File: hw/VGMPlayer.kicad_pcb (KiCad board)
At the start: 4 copper layers, 40 x 67 mm, 99 parts, among them J1 Micro_SD_Card, J2 EarPiece, P1 USB_C_Receptacle_16P, P2 SWD, P3 BATT, P5 ICSP, P6 CODEC, Q1 AO3401A, Q2 AO3401A, Q3 2N7002, Q4 2N7002, U1 RP2040, U2 W25QxxJVZP, U3 LP5907MFX-3.3, U4 WM8978, U5 MCP73831-OT, U6 PIC16F1503-IMG, U7 LP5907MFX-3.3, Y1 12MHz

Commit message: Rename button labels
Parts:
- S1: value L -> M
- S2: value R -> P

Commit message: Using Linux Kicad 6.0.1
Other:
- net class Default removed
- net class Power removed

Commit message: V4 hardware
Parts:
- removed C14: 1u, BZ_Capacitor:C_0603
- removed the C17 at (138.4, 109.3)
- removed the C19 at (136.6, 119.0)
- removed the C23 at (131.6, 111.7)
- removed the C24 at (134.8, 116.8)
- removed the C27 at (140.1, 118.8)
- removed the C30 at (145.1, 134.2)
- removed JP1: Jumper-NC, BZ_Misc:Jumper-Solder
- removed JP2, JP3: Jumper-NO, BZ_Misc:Jumper-Solder
- removed R13: 1K, BZ_Resistor:R_0402
- removed the U3 at (134.3, 113.9)
- added C20: 1u, BZ_Capacitor:C_0603, B.Cu at (135.0, 120.8)
- added U4: MAX9890BETA, BZ_Standard_IC:TDFN-8-1EP_3x3x0.65P_EP2.3x1.5, B.Cu at (136.5, 118.1)
- added kibuzzard-62236962: G***, kibuzzard-62236962, F.Cu at (157.1, 141.0)
- C15: renamed from C25; value 10u -> 4.7u
- C16: renamed from C18; value 10u -> 4.7u
- C17: renamed from C20; value 10u -> 4.7u
- C18: renamed from C22; value 10u -> 4.7u
- C19: renamed from C26; value 10u -> 4.7u
- S1: value M -> B
- S2: value P -> F
- S5: value RESET -> P; footprint BZ_Switch:SW-PUSH_4x3x2H -> VGMPlayer:MultiButton; moved to F.Cu
- moved C15 13.0 mm to (142.3, 108.7), turned to 90 degrees
- moved S3 13.0 mm to (140.0, 132.3), turned to 90 degrees
- moved C18 11.2 mm to (132.3, 115.9), turned to 180 degrees
- moved C19 8.18 mm to (132.3, 114.5), turned to 180 degrees
- moved S5 8.02 mm to (160.0, 123.5), turned to -90 degrees
- moved C17 6.49 mm to (132.3, 113.1), turned to 180 degrees
- moved S2 5.03 mm to (160.0, 132.3)
- moved S1 4.27 mm to (140.0, 123.5)
- moved C16 3.95 mm to (143.7, 108.7)
- moved C21 3.94 mm to (138.1, 120.8), turned to 180 degrees
- moved S4 3.10 mm to (150.0, 127.9)
- moved U3 2.92 mm to (138.3, 111.6), turned to 45 degrees
- moved FB1 2.31 mm to (132.0, 110.3), turned to 180 degrees
- moved R15 1.60 mm to (143.1, 133.4)
- moved R17 1.60 mm to (143.1, 135.0)
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- renumbered C28 to C22, C29 to C23, C16 to C24, C31 to C25, C33 to C26, C34 to C27, C35 to C28, C32 to C29, C36 to C30, U4 to U3
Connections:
- C15 pad 1: VDDA -> 3V3
- C17 pad 1: VDDA -> /AVDD
- C18 pad 1: Net-(C21-Pad1) -> VIN
- C22 pad 1: Net-(C28-Pad1) -> Net-(C22-Pad1)
- C23 pad 1: Net-(C29-Pad1) -> Net-(C23-Pad1)
- C26 pad 1: Net-(C33-Pad1) -> VIN
- FB1 pad 1: Net-(C21-Pad1) -> /AVDD
- FB1 pad 2: VIN -> 3V3
- P1 pad A8: (no net) -> unconnected-(P1-PadA8)
- P1 pad B8: (no net) -> unconnected-(P1-PadB8)
- P2 pad 6: (no net) -> unconnected-(P2-Pad6)
- P2 pad 7: (no net) -> unconnected-(P2-Pad7)
- P5 pad 6: (no net) -> unconnected-(P5-Pad6)
- Q2 pad 3: Net-(C33-Pad1) -> VIN
- U1 pad 29: (no net) -> unconnected-(U1-Pad29)
- U1 pad 30: (no net) -> unconnected-(U1-Pad30)
- U1 pad 31: Net-(R13-Pad2) -> /OUTEN
- U1 pad 38: (no net) -> /JACK_DET
- U1 pad 39: (no net) -> unconnected-(U1-Pad39)
- U1 pad 40: (no net) -> unconnected-(U1-Pad40)
- U1 pad 41: (no net) -> unconnected-(U1-Pad41)
- U3 pad 1: (no net) -> unconnected-(U3-Pad1)
- U3 pad 15: (no net) -> unconnected-(U3-Pad15)
- U3 pad 19: /BEEP -> unconnected-(U3-Pad19)
- U3 pad 2: (no net) -> unconnected-(U3-Pad2)
- U3 pad 20: (no net) -> unconnected-(U3-Pad20)
- U3 pad 21: (no net) -> unconnected-(U3-Pad21)
- U3 pad 22: (no net) -> unconnected-(U3-Pad22)
- U3 pad 26: Net-(C21-Pad1) -> VIN
- U3 pad 29: Net-(C28-Pad1) -> Net-(U3-Pad29)
- U3 pad 30: Net-(C29-Pad1) -> Net-(U3-Pad30)
- U3 pad 31: VDDA -> /AVDD
- U3 pad 32: (no net) -> unconnected-(U3-Pad32)
- U3 pad 4: (no net) -> unconnected-(U3-Pad4)
- U3 pad 5: (no net) -> unconnected-(U3-Pad5)
- U3 pad 6: (no net) -> unconnected-(U3-Pad6)
- U3 pad 9: (no net) -> unconnected-(U3-Pad9)
- U7 pad 1: Net-(C33-Pad1) -> VIN
- U7 pad 3: Net-(C33-Pad1) -> VIN
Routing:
- net 3V3: track 109.5 -> 156.2 mm
- net Net-(C21-Pad1): track 31.0 -> 1.95 mm, vias 2 -> 0
- net VIN: track 23.6 -> 45.6 mm
- net /OUTEN: track 0.00 -> 21.4 mm, vias 0 -> 2
- net /AVDD: track 0.00 -> 16.9 mm, vias 0 -> 2
- net Net-(R13-Pad2): track 15.8 -> 0.00 mm, vias 2 -> 0
- net Net-(C33-Pad1): track 14.7 -> 0.00 mm, vias 2 -> 0
- net VDDA: track 12.2 -> 0.00 mm
- net /ICSPCLK: track 43.5 -> 55.7 mm
- net Net-(C29-Pad1): track 11.8 -> 0.00 mm
- net Net-(C28-Pad1): track 10.8 -> 0.00 mm
- net Net-(U3-Pad29): track 0.00 -> 8.80 mm, vias 0 -> 2
- net Net-(C23-Pad1): track 0.00 -> 8.52 mm
- net Net-(C22-Pad1): track 0.00 -> 7.86 mm
- net /VPP: track 34.4 -> 41.9 mm
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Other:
- rule solder_mask_min_width: 0.08 -> 0.2
- board text added: "20220305"
- board text removed: "20210714"

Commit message: V4 hardware send for JLC
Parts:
- removed the C27 at (155.6, 96.8)
- removed Q2: AO3401A, BZ_Standard_IC:SOT-23-3
- removed R20: 100K, BZ_Resistor:R_0402
- added C29: 4.7u, BZ_Capacitor:C_0603, B.Cu at (156.1, 95.3)
- added R13: 10K, BZ_Resistor:R_0402, B.Cu at (132.3, 118.0)
- C26: value 1u -> 4.7u
- R21: value 10K -> 100K
- S1: value B -> U
- S2: value F -> B
- S3: value U -> D
- S4: value D -> P
- S5: value P -> F
- U7: value LP5907MFX-3.3 -> XC6220B331MR
- moved C25 7.52 mm to (156.1, 104.0), turned to 180 degrees
- moved C26 4.17 mm to (156.1, 97.4), turned to 180 degrees
- moved R18 2.58 mm to (159.4, 98.4), turned to -90 degrees
- moved S1 2.26 mm to (139.5, 121.3)
- moved S5 2.26 mm to (160.5, 121.3)
- moved D2 1.90 mm to (159.2, 102.5)
- moved R21 1.60 mm to (153.0, 104.2), turned to -90 degrees
- moved R23 1.50 mm to (153.0, 102.1)
- moved R24 1.40 mm to (153.0, 100.0)
- moved C28 1.30 mm to (153.0, 97.9)
- moved S4 1.00 mm to (150.0, 126.9)
- moved U7 1.00 mm to (156.1, 100.7)
- moved S2 0.54 mm to (160.5, 132.5)
- moved S3 0.54 mm to (139.5, 132.5)
- moved R15 0.50 mm to (143.1, 132.9)
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- renumbered C15 to C14, C16 to C15, C17 to C16, C18 to C17, C20 to C18, C21 to C19, C19 to C20, C22 to C21, C23 to C22, C24 to C23, C25 to C24, C28 to C25, C29 to C27, C30 to C28
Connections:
- C17 pad 1: VIN -> /AVDD
- C25 pad 1: 3V3 -> VRAW
- C26 pad 1: VIN -> 3V3
- R21 pad 1: Net-(Q2-Pad1) -> Net-(R21-Pad1)
- R21 pad 2: Net-(R21-Pad2) -> GND
- U3 pad 26: VIN -> /AVDD
- U6 pad 7: Net-(R21-Pad2) -> Net-(R21-Pad1)
- U7 pad 1: VIN -> VRAW
- U7 pad 3: VIN -> Net-(R21-Pad1)
- U7 pad 4: Net-(C27-Pad1) -> unconnected-(U7-Pad4)
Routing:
- net VIN: track 45.6 -> 0.00 mm, vias 2 -> 0
- net 3V3: track 156.2 -> 141.1 mm, vias 15 -> 16
- net GND: track 219.3 -> 230.7 mm, vias 79 -> 77
- net Net-(Q2-Pad1): track 6.19 -> 0.00 mm
- net Net-(R21-Pad1): track 0.00 -> 5.33 mm
- net VRAW: track 45.3 -> 41.5 mm
- net /OUTEN: track 21.4 -> 25.0 mm, vias 2 -> 3
- net Net-(R21-Pad2): track 3.19 -> 0.00 mm
- net /AVDD: track 16.9 -> 20.0 mm, vias 2 -> 3
- net /VPP: track 41.9 -> 39.4 mm
- net /BATT: track 33.3 -> 31.4 mm
- net Net-(C28-Pad1): track 10.1 -> 8.37 mm
- net Net-(C27-Pad1): track 1.35 -> 0.00 mm
- net /ICSPDAT: track 56.6 -> 55.4 mm
- net Net-(S4-Pad2): track 30.1 -> 29.1 mm
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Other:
- rule pad_to_mask_clearance: 0.05 -> 0
- board text added: "20220306"
- board text removed: "20220305"

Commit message: Use new iPhone8 measurement
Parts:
- U5: value MCP73831-OT -> MCP73832-OT
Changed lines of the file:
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@@
       (effects (font (size 0.8 0.8) (thickness 0.15)) (justify mirror))
     )
-    (fp_text value "MCP73831-OT" (at 0 -2.6) (layer "B.Fab") hide
+    (fp_text value "MCP73832-OT" (at 0 -2.6) (layer "B.Fab") hide
       (effects (font (size 0.8 0.8) (thickness 0.15)) (justify mirror))
     )

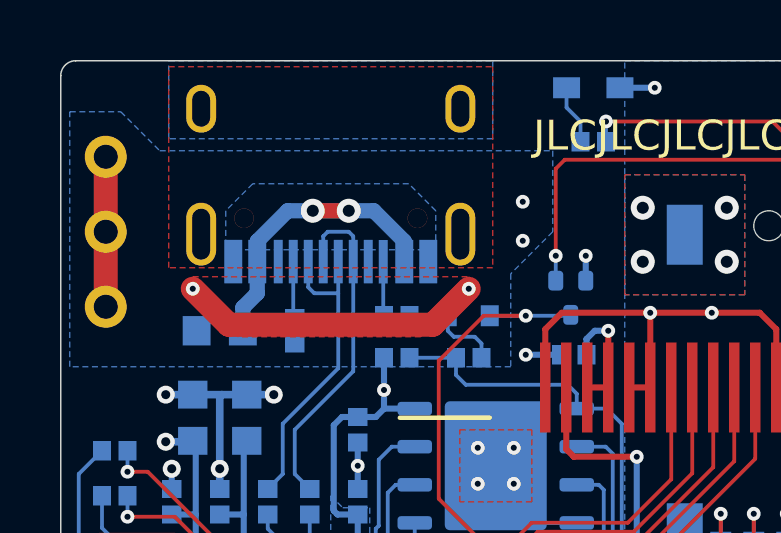
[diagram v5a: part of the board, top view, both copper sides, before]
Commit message: Update switch names
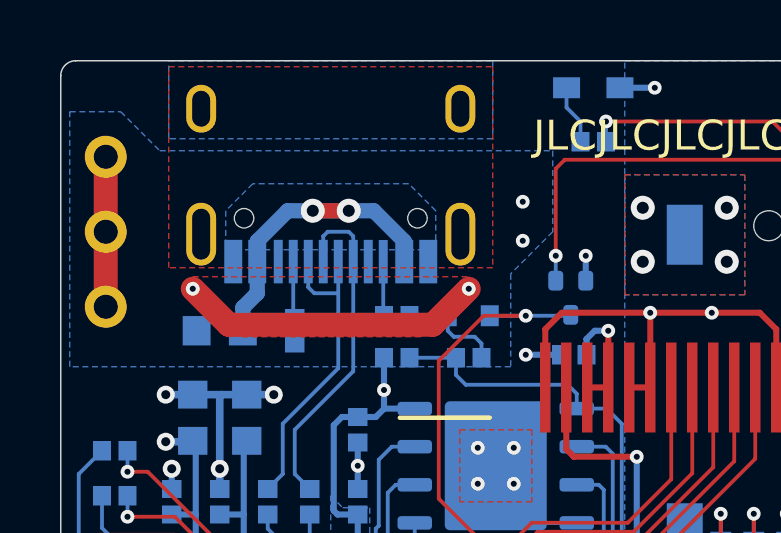
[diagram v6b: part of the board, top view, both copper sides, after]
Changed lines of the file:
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@@
     (property "Sheetname" "")
     (attr smd)
-    (fp_text reference "P1" (at 0 9.6) (layer "B.SilkS") hide
+    (fp_text reference "P1" (at 0 9.6 180) (layer "B.SilkS") hide
       (effects (font (size 0.8 0.8) (thickness 0.15)) (justify mirror))
     )
-    (fp_text value "USB_C_Receptacle_16P" (at 0 -1.5) (layer "B.Fab") hide
+    (fp_text value "USB_C_Receptacle_16P" (at 0 -1.5 180) (layer "B.Fab") hide
       (effects (font (size 1 1) (thickness 0.15)) (justify mirror))
     )
-    (fp_text user "${REFERENCE}" (at 0 6.7) (layer "B.Fab")
+    (fp_text user "${REFERENCE}" (at 0 6.7 180) (layer "B.Fab")
       (effects (font (size 0.8 0.8) (thickness 0.15)) (justify mirror))
     )
@@
     (fp_line (start 4.47 7.3) (end -4.47 7.3) (layer "B.Fab") (width 0.1))
     (fp_line (start -4.47 7.3) (end -4.47 0) (layer "B.Fab") (width 0.1))
-    (pad "A1" smd rect locked (at -3.25 7.695) (size 0.6 1.45) (layers "B.Cu" "B.Paste" "B.Mask")
+    (pad "" np_thru_hole oval (at 2.89 6.25) (size 0.65 0.65) (drill 0.65) (layers F&B.Cu *.Mask))
+    (pad "" np_thru_hole oval (at -2.89 6.25) (size 0.65 0.65) (drill 0.65) (layers F&B.Cu *.Mask))
+    (pad "A1" smd rect (at -3.25 7.695) (size 0.6 1.45) (layers "B.Cu" "B.Paste" "B.Mask")
       (net 1 "GND") (pinfunction "GND") (pintype "passive"))
-    (pad "A4" smd rect locked (at -2.45 7.695) (size 0.6 1.45) (layers "B.Cu" "B.Paste" "B.Mask")
+    (pad "A4" smd rect (at -2.45 7.695) (size 0.6 1.45) (layers "B.Cu" "B.Paste" "B.Mask")
       (net 2 "VUSB") (pinfunction "VBUS") (pintype "passive"))
-    (pad "A5" smd rect locked (at -1.25 7.695) (size 0.3 1.45) (layers "B.Cu" "B.Paste" "B.Mask")
+    (pad "A5" smd rect (at -1.25 7.695) (size 0.3 1.45) (layers "B.Cu" "B.Paste" "B.Mask")
       (net 8 "Net-(P1-PadA5)") (pinfunction "CC1") (pintype "bidirectional"))
-    (pad "A6" smd rect locked (at -0.25 7.695) (size 0.3 1.45) (layers "B.Cu" "B.Paste" "B.Mask")
+    (pad "A6" smd rect (at -0.25 7.695) (size 0.3 1.45) (layers "B.Cu" "B.Paste" "B.Mask")
       (net 6 "Net-(P1-PadA6)") (pinfunction "D+") (pintype "bidirectional"))
-    (pad "A7" smd rect locked (at 0.25 7.695) (size 0.3 1.45) (layers "B.Cu" "B.Paste" "B.Mask")
+    (pad "A7" smd rect (at 0.25 7.695) (size 0.3 1.45) (layers "B.Cu" "B.Paste" "B.Mask")
       (net 5 "Net-(P1-PadA7)") (pinfunction "D-") (pintype "bidirectional"))
-    (pad "A8" smd rect locked (at 1.25 7.695) (size 0.3 1.45) (layers "B.Cu" "B.Paste" "B.Mask")
+    (pad "A8" smd rect (at 1.25 7.695) (size 0.3 1.45) (layers "B.Cu" "B.Paste" "B.Mask")
       (net 76 "unconnected-(P1-PadA8)") (pinfunction "SBU1") (pintype "bidirectional+no_connect"))
-    (pad "A9" smd rect locked (at 2.45 7.695) (size 0.6 1.45) (layers "B.Cu" "B.Paste" "B.Mask")
+    (pad "A9" smd rect (at 2.45 7.695) (size 0.6 1.45) (layers "B.Cu" "B.Paste" "B.Mask")
       (net 2 "VUSB") (pinfunction "VBUS") (pintype "passive"))
-    (pad "A12" smd rect locked (at 3.25 7.695) (size 0.6 1.45) (layers "B.Cu" "B.Paste" "B.Mask")
+    (pad "A12" smd rect (at 3.25 7.695) (size 0.6 1.45) (layers "B.Cu" "B.Paste" "B.Mask")
       (net 1 "GND") (pinfunction "GND") (pintype "passive"))
-    (pad "B1" smd rect locked (at 3.25 7.695) (size 0.6 1.45) (layers "B.Cu" "B.Paste" "B.Mask")
+    (pad "B1" smd rect (at 3.25 7.695) (size 0.6 1.45) (layers "B.Cu" "B.Paste" "B.Mask")
       (net 1 "GND") (pinfunction "GND") (pintype "passive"))
-    (pad "B4" smd rect locked (at 2.45 7.695) (size 0.6 1.45) (layers "B.Cu" "B.Paste" "B.Mask")
+    (pad "B4" smd rect (at 2.45 7.695) (size 0.6 1.45) (layers "B.Cu" "B.Paste" "B.Mask")
       (net 2 "VUSB") (pinfunction "VBUS") (pintype "passive"))
-    (pad "B5" smd rect locked (at 1.75 7.7) (size 0.3 1.45) (layers "B.Cu" "B.Paste" "B.Mask")
+    (pad "B5" smd rect (at 1.75 7.7) (size 0.3 1.45) (layers "B.Cu" "B.Paste" "B.Mask")
       (net 7 "Net-(P1-PadB5)") (pinfunction "CC2") (pintype "bidirectional"))
-    (pad "B6" smd rect locked (at 0.75 7.695) (size 0.3 1.45) (layers "B.Cu" "B.Paste" "B.Mask")
+    (pad "B6" smd rect (at 0.75 7.695) (size 0.3 1.45) (layers "B.Cu" "B.Paste" "B.Mask")
       (net 6 "Net-(P1-PadA6)") (pinfunction "D+") (pintype "bidirectional"))
-    (pad "B7" smd rect locked (at -0.75 7.695) (size 0.3 1.45) (layers "B.Cu" "B.Paste" "B.Mask")
+    (pad "B7" smd rect (at -0.75 7.695) (size 0.3 1.45) (layers "B.Cu" "B.Paste" "B.Mask")
       (net 5 "Net-(P1-PadA7)") (pinfunction "D-") (pintype "bidirectional"))
-    (pad "B8" smd rect locked (at -1.75 7.695) (size 0.3 1.45) (layers "B.Cu" "B.Paste" "B.Mask")
+    (pad "B8" smd rect (at -1.75 7.695) (size 0.3 1.45) (layers "B.Cu" "B.Paste" "B.Mask")
       (net 77 "unconnected-(P1-PadB8)") (pinfunction "SBU2") (pintype "bidirectional+no_connect"))
-    (pad "B9" smd rect locked (at -2.45 7.695) (size 0.6 1.45) (layers "B.Cu" "B.Paste" "B.Mask")
+    (pad "B9" smd rect (at -2.45 7.695) (size 0.6 1.45) (layers "B.Cu" "B.Paste" "B.Mask")
       (net 2 "VUSB") (pinfunction "VBUS") (pintype "passive"))
-    (pad "B12" smd rect locked (at -3.25 7.695) (size 0.6 1.45) (layers "B.Cu" "B.Paste" "B.Mask")
+    (pad "B12" smd rect (at -3.25 7.695) (size 0.6 1.45) (layers "B.Cu" "B.Paste" "B.Mask")
       (net 1 "GND") (pinfunction "GND") (pintype "passive"))
-    (pad "M" thru_hole oval locked (at 2.89 6.25) (size 0.65 0.65) (drill 0.65) (layers *.Cu *.Mask))
-    (pad "M" thru_hole oval locked (at -2.89 6.25) (size 0.65 0.65) (drill 0.65) (layers *.Cu *.Mask))
-    (pad "S1" thru_hole oval locked (at 4.32 6.78) (size 1 2.1) (drill oval 0.6 1.7) (layers *.Cu *.Mask)
+    (pad "S1" thru_hole oval (at 4.32 6.78) (size 1 2.1) (drill oval 0.6 1.7) (layers *.Cu *.Mask)
       (net 58 "Net-(P1-PadS1)") (pinfunction "SHIELD") (pintype "passive"))
-    (pad "S2" thru_hole oval locked (at -4.32 6.78) (size 1 2.1) (drill oval 0.6 1.7) (layers *.Cu *.Mask)
+    (pad "S2" thru_hole oval (at -4.32 6.78) (size 1 2.1) (drill oval 0.6 1.7) (layers *.Cu *.Mask)
       (net 58 "Net-(P1-PadS1)") (pinfunction "SHIELD") (pintype "passive"))
-    (pad "S3" thru_hole oval locked (at -4.32 2.6) (size 1 1.6) (drill oval 0.6 1.2) (layers *.Cu *.Mask)
+    (pad "S3" thru_hole oval (at -4.32 2.6) (size 1 1.6) (drill oval 0.6 1.2) (layers *.Cu *.Mask)
       (net 58 "Net-(P1-PadS1)") (pinfunction "SHIELD") (pintype "passive"))
-    (pad "S4" thru_hole oval locked (at 4.32 2.6) (size 1 1.6) (drill oval 0.6 1.2) (layers *.Cu *.Mask)
+    (pad "S4" thru_hole oval (at 4.32 2.6) (size 1 1.6) (drill oval 0.6 1.2) (layers *.Cu *.Mask)
       (net 58 "Net-(P1-PadS1)") (pinfunction "SHIELD") (pintype "passive"))
     (model "${KIUSR3DMOD}/Connector.3dshapes/HRO_TYPE-C-31-M-12.wrl"
